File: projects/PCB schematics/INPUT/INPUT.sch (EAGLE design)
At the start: 100 parts, among them IC1 OP11D, IC10 74AHC1G32DCK, IC11 OP11D, IC13 OP11D, IC14 74AHC1G32DCK, IC17 OP11D, IC18 74AHC1G32DCK, IC19 OP11D, IC2 OP11D, IC20 OP11D, IC3 OP11D, IC4 OP11D, IC5 OP11D, IC6 74AHC1G32DCK, IC7 OP11D, IC8 OP11D, IC9 74AHC1G32DCK

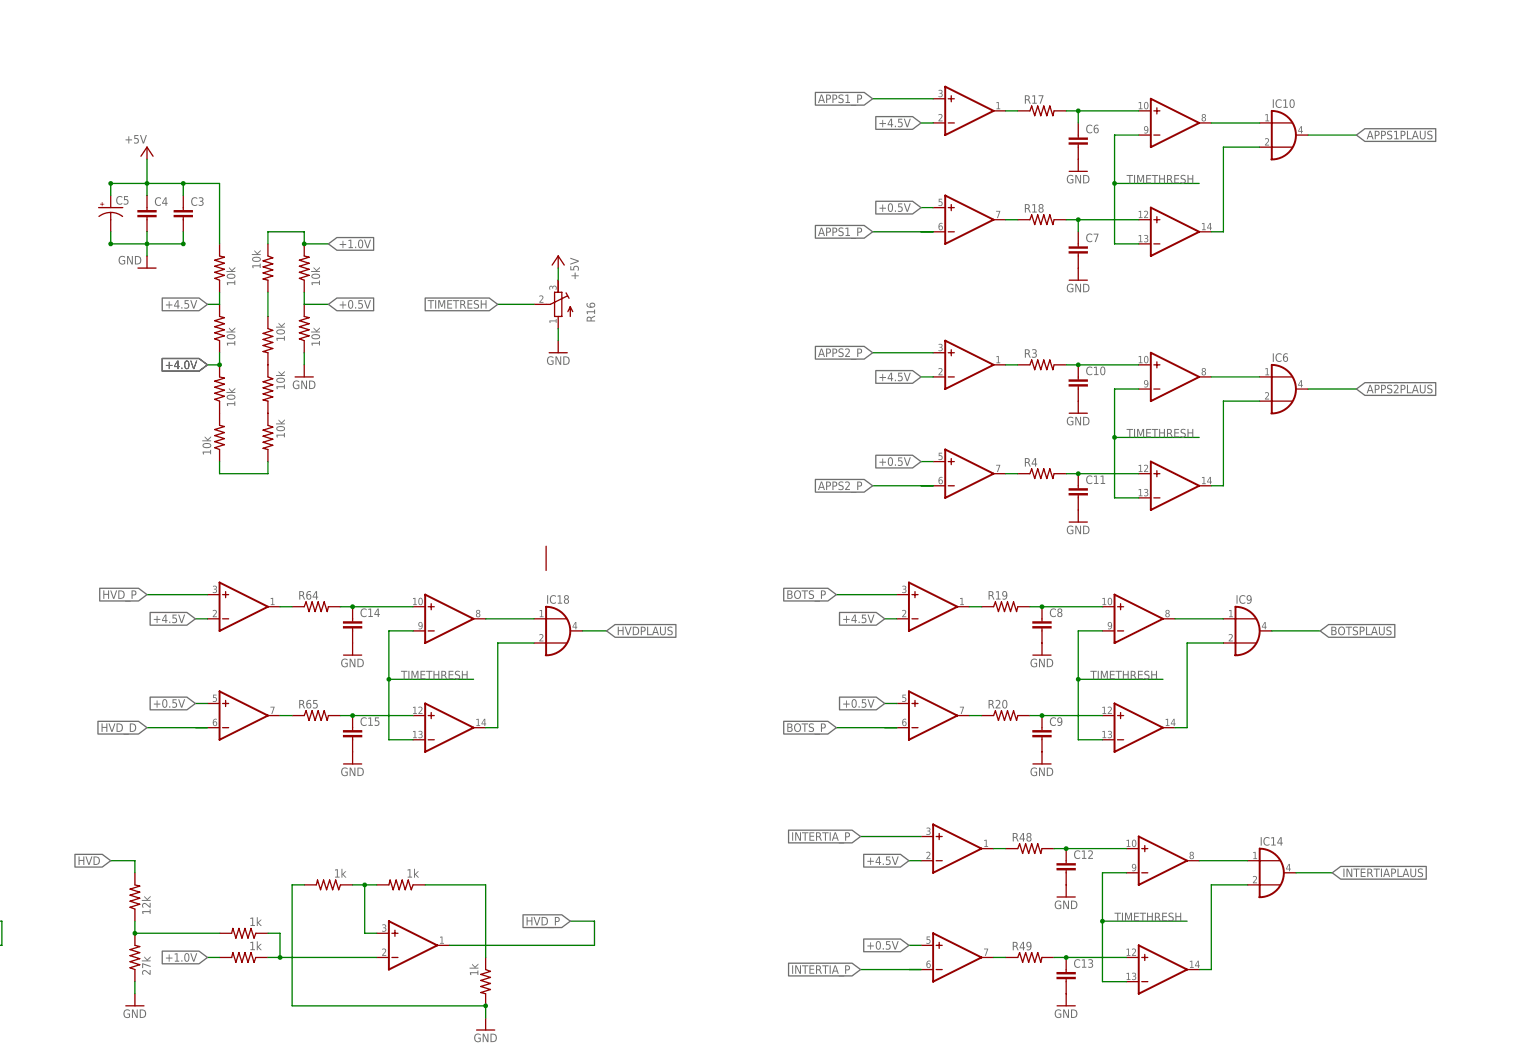
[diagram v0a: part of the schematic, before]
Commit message: PROJ - Added IMD, OUTPUT.
Additional changes made to INPUT.
OUTPUT board added for ECU/motor controller signal processing.
IMD added for IMD fuse board. Rules may require fusing IMD. Might as well.
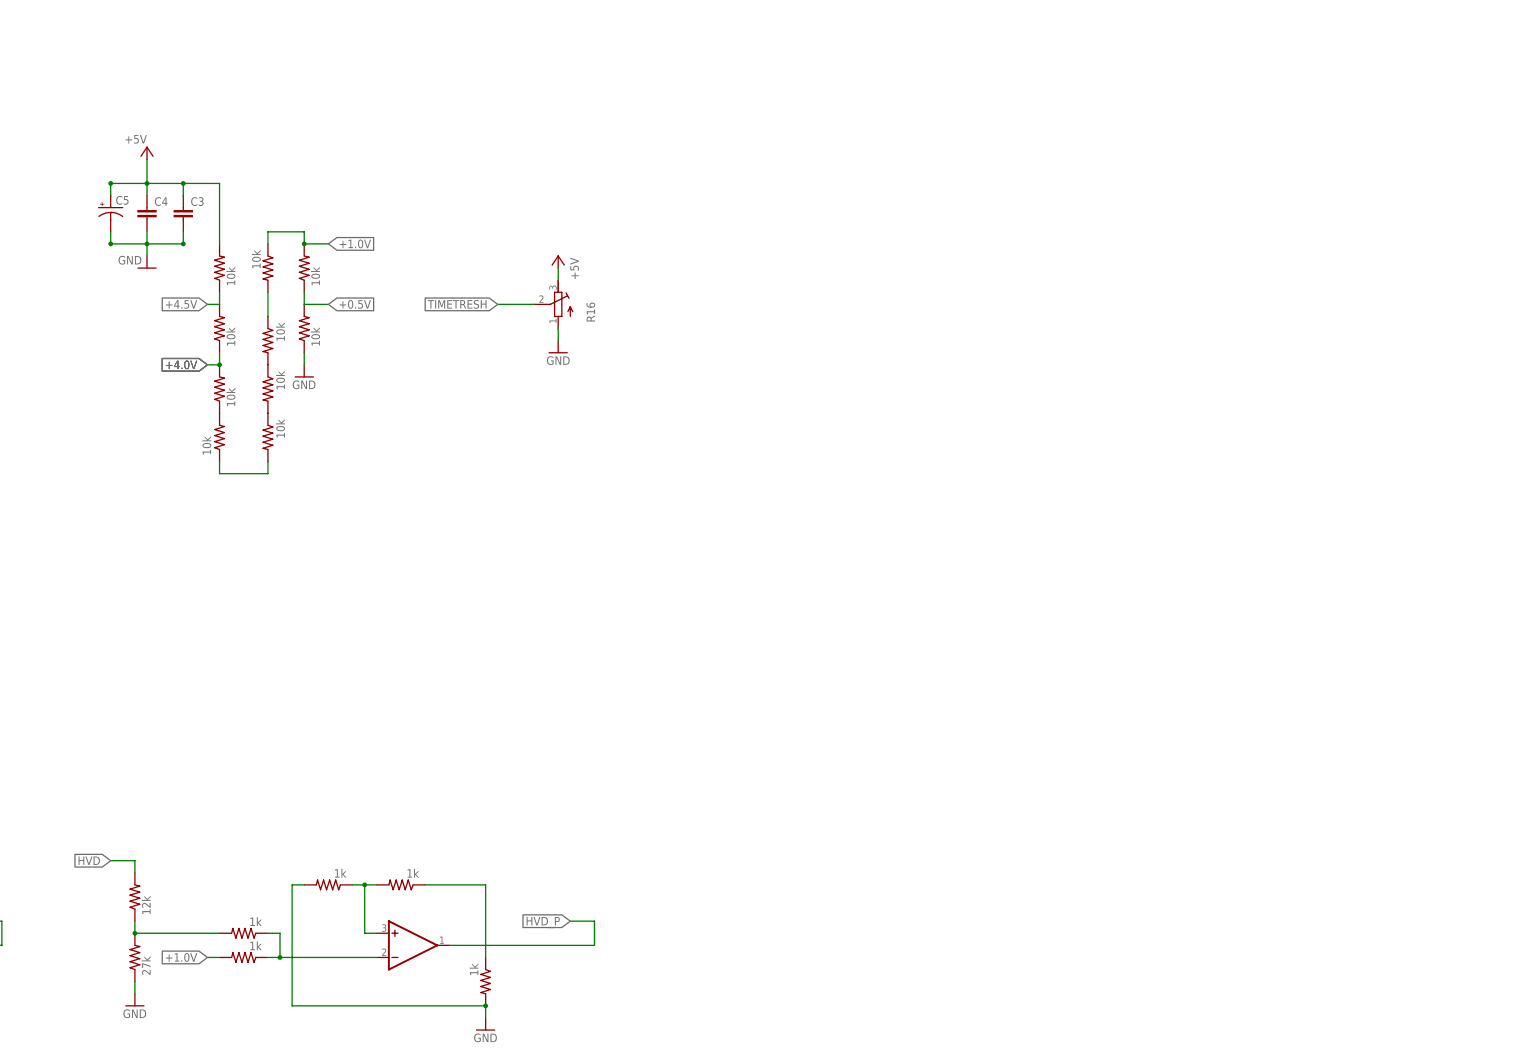
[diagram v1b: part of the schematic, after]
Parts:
- removed C10, C11, C12, C13, C14, C15, C6, C7, C8, C9: (no value), rcl:C-EUC0805
- removed IC1, IC13, IC17, IC4, IC5: OP11D, linear:OP11D
- removed IC10, IC14, IC18, IC6, IC9: 74AHC1G32DCK, 74xx-little-de:74AHC1G32DCK
- removed R17, R18, R19, R20, R3, R4, R48, R49, R64, R65: (no value), rcl:R-US_R0805
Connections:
- removed net APPS1PLAUS: IC10A.O
- removed net APPS2PLAUS: IC6A.O
- removed net BOTSPLAUS: IC9A.O
- removed net HVDPLAUS: IC18A.O
- removed net HVD_D: IC17B.-IN
- removed net INTERTIAPLAUS: IC14A.O
- removed net INTERTIA_P: IC13A.+IN, IC13B.-IN
- removed net N$12: C6.1, IC5C.+IN, R17.2
- removed net N$13: C7.1, IC5D.+IN, R18.2
- removed net N$14: IC5B.OUT, R18.1
- removed net N$15: IC1A.OUT, R3.1
- removed net N$16: C10.1, IC1C.+IN, R3.2
- removed net N$17: C11.1, IC1D.+IN, R4.2
- removed net N$18: IC1B.OUT, R4.1
- removed net N$20: C8.1, IC4C.+IN, R19.2
- removed net N$23: C9.1, IC4D.+IN, R20.2
- removed net N$24: IC4B.OUT, R20.1
- removed net N$26: IC1C.OUT, IC6A.I0
- removed net N$27: IC1D.OUT, IC6A.I1
- removed net N$3: IC4A.OUT, R19.1
- removed net N$34: IC4C.OUT, IC9A.I0
- removed net N$35: IC4D.OUT, IC9A.I1
- removed net N$42: IC13A.OUT, R48.1
- removed net N$43: C12.1, IC13C.+IN, R48.2
- removed net N$46: IC10A.I0, IC5C.OUT
- removed net N$47: IC10A.I1, IC5D.OUT
- removed net N$48: C13.1, IC13D.+IN, R49.2
- removed net N$49: IC13B.OUT, R49.1
- removed net N$50: IC13C.OUT, IC14A.I0
- removed net N$51: IC13D.OUT, IC14A.I1
- removed net N$6: IC5A.OUT, R17.1
- removed net N$60: IC17A.OUT, R64.1
- removed net N$61: C14.1, IC17C.+IN, R64.2
- removed net N$62: C15.1, IC17D.+IN, R65.2
- removed net N$63: IC17B.OUT, R65.1
- removed net N$64: IC17C.OUT, IC18A.I0
- removed net N$65: IC17D.OUT, IC18A.I1
- removed net TIMETHRESH: IC13C.-IN, IC13D.-IN, IC17C.-IN, IC17D.-IN, IC1C.-IN, IC1D.-IN, IC4C.-IN, IC4D.-IN, IC5C.-IN, IC5D.-IN
- net +0.5V: no longer IC13B.+IN, IC17B.+IN, IC1B.+IN, IC4B.+IN, IC5B.+IN
- net +4.5V: no longer IC13A.-IN, IC17A.-IN, IC1A.-IN, IC4A.-IN, IC5A.-IN
- net APPS1_P: no longer IC5A.+IN, IC5B.-IN
- net APPS2_P: no longer IC1A.+IN, IC1B.-IN
- net BOTS_P: no longer IC4A.+IN, IC4B.-IN
- net GND: no longer C10.2, C11.2, C12.2, C13.2, C14.2, C15.2, C6.2, C7.2, C8.2, C9.2
- net HVD_P: no longer IC17A.+IN
